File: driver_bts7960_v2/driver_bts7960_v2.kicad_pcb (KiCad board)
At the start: 2 copper layers, 56.4 x 50.7 mm, 31 parts, among them J1 Motor_1, J2 Alimentacion, J6 Motor_2, J7 Conn_02x04_Odd_Even, U1 BTS7960B, U2 BTS7960B, U3 BTS7960B, U4 BTS7960B

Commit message: v2
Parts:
- J1, J6: footprint Connector_AMASS:AMASS_XT30PW-M_1x02_P2.50mm_Horizontal -> Connector_AMASS:AMASS_XT30UPB-F_1x02_P5.0mm_Vertical
- moved REF** 9.10 mm to (161.7, 38.4)
- moved REF** 9.07 mm to (111.9, 38.4)
- moved C5 5.89 mm to (136.8, 72.5), turned to 0 degrees
- moved J2 4.63 mm to (152.1, 73.8)
- moved J7 3.45 mm to (127.7, 70.2)
- moved J1 1.46 mm to (128.6, 38.4), turned to 180 degrees
- moved J6 1.46 mm to (144.5, 38.4), turned to 180 degrees
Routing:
- net +24V: track 154.6 -> 86.3 mm
- net ENABLE_2: track 42.4 -> 48.5 mm
- net PWM_C: track 28.3 -> 33.3 mm
- net GND: track 160.3 -> 165.0 mm
- net PWM_B: track 14.2 -> 18.0 mm
- net PWM_A: track 5.91 -> 9.24 mm
- net PWM_D: track 14.1 -> 17.0 mm
- net Net-(J6-Pin_2): track 7.21 -> 8.67 mm
- net IS_1: track 51.2 -> 52.6 mm
- net Net-(J1-Pin_1): track 7.24 -> 8.66 mm
- net Net-(J1-Pin_2): track 22.1 -> 23.3 mm
- net Net-(J6-Pin_1): track 12.5 -> 13.6 mm
- net IS_2: track 79.2 -> 80.1 mm
- net ENABLE_1: track 21.3 -> 21.9 mm
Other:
- board size 56.4 x 50.7 mm -> 56.4 x 42.1 mm

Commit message: .
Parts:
- moved REF** 0.27 mm to (111.9, 73.6)
- moved REF** 0.21 mm to (161.7, 73.6)
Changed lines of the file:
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@@
 	(footprint "MountingHole:MountingHole_3.2mm_M3_DIN965_Pad_TopBottom"
 		(layer "F.Cu")
-		(at 111.7 73.775)
+		(at 111.9 73.6)
 		(descr "Mounting Hole 3.2mm, M3, DIN965")
 		(tags "mounting hole 3.2mm m3 din965")
@@
 	(footprint "MountingHole:MountingHole_3.2mm_M3_DIN965_Pad_TopBottom"
 		(layer "F.Cu")
-		(at 161.875 73.75)
+		(at 161.725 73.6)
 		(descr "Mounting Hole 3.2mm, M3, DIN965")
 		(tags "mounting hole 3.2mm m3 din965")
@@
 		(polygon
 			(pts
-				(xy 108.6 52.4695) (xy 159.3 51.963674) (xy 159.3 69.04) (xy 108.6 69.04)
+				(xy 108.6 52.4695) (xy 164.975 51.907056) (xy 164.975 76.87) (xy 108.6 76.87)
 			)
 		)

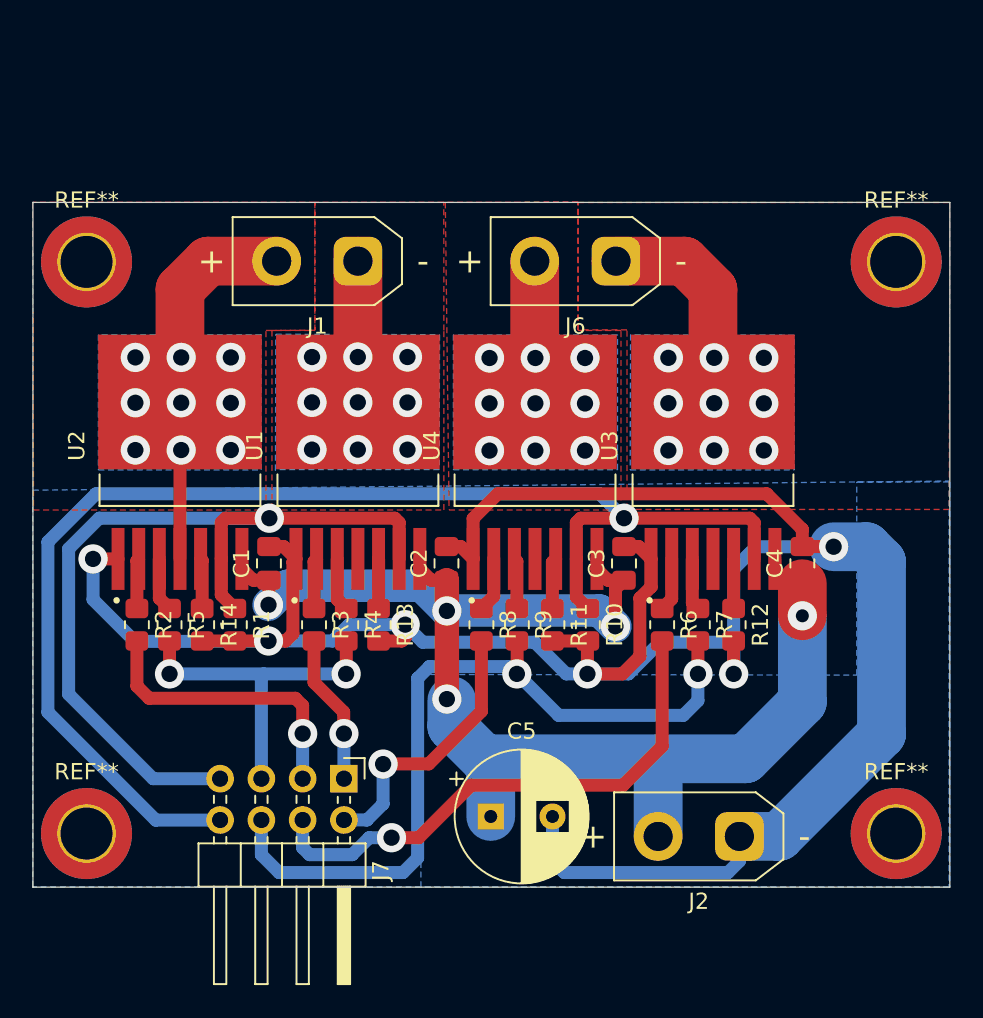
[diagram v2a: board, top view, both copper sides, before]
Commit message: v2 terminado con 74hc244
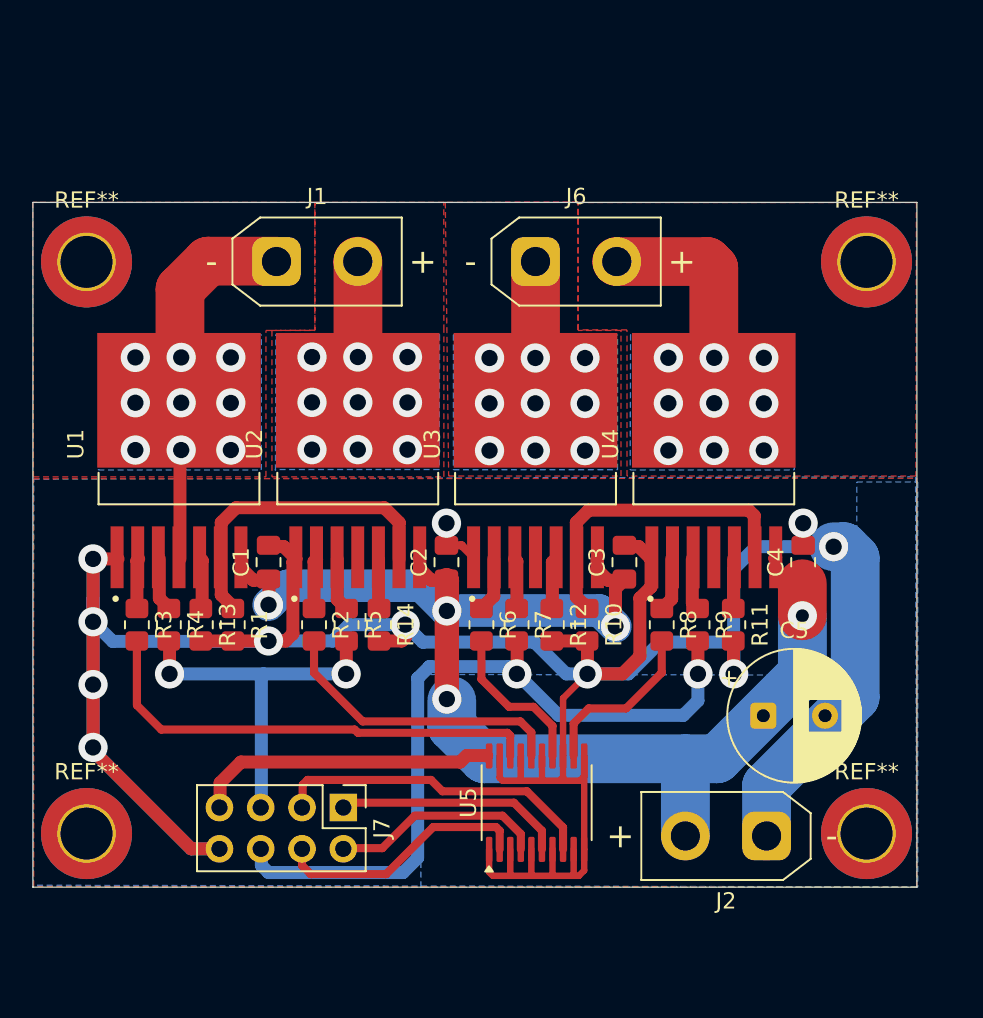
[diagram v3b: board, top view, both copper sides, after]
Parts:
- added U5: 74HC244, Package_SO:SSOP-20_4.4x6.5mm_P0.65mm, F.Cu at (139.6, 71.7)
- J7: footprint Connector_PinHeader_2.54mm:PinHeader_2x04_P2.54mm_Horizontal -> Connector_PinHeader_2.54mm:PinHeader_2x04_P2.54mm_Vertical
- moved C5 17.9 mm to (153.5, 66.3)
- moved R12 11.2 mm to (140.5, 60.8)
- moved R7 11.2 mm to (138.4, 60.8)
- moved R11 11.1 mm to (151.7, 60.8)
- moved R6 11.1 mm to (136.2, 60.8)
- moved R9 11.1 mm to (149.5, 60.8)
- moved R8 11.1 mm to (147.3, 60.8)
- moved U1 11.0 mm to (117.6, 50.6)
- moved U4 11.0 mm to (150.5, 50.6)
- moved U2 10.9 mm to (128.6, 50.6)
- moved R13 10.9 mm to (118.9, 60.8)
- moved U3 10.9 mm to (139.5, 50.6)
- moved R4 10.9 mm to (117.0, 60.8)
- moved R2 10.9 mm to (125.9, 60.8)
- moved R3 10.9 mm to (115.0, 60.8)
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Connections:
- J7 pad 1: PWM_A -> PWM_C
- J7 pad 2: PWM_D -> PWM_B
- J7 pad 3: PWM_B -> PWM_D
- J7 pad 4: PWM_C -> PWM_A
- J7 pad 7: IS_1 -> +5V
- J7 pad 8: IS_2 -> GND
- R1 pad 1: IS_1 -> Net-(U1-IS)
- R10 pad 1: IS_2 -> Net-(U3-IS)
- R2 pad 2: PWM_B -> OUT_B
- R3 pad 2: PWM_A -> OUT_A
- R6 pad 2: PWM_C -> OUT_C
- R8 pad 2: PWM_D -> OUT_D
- U1 pad 6: IS_1 -> Net-(U1-IS)
- U2 pad 6: IS_1 -> Net-(U1-IS)
- U3 pad 6: IS_2 -> Net-(U3-IS)
- U4 pad 6: IS_2 -> Net-(U3-IS)
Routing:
- net IS_2: track 80.1 -> 0.00 mm, vias 1 -> 0
- net IS_1: track 52.6 -> 0.00 mm, vias 1 -> 0
- net GND: track 165.0 -> 201.7 mm, vias 6 -> 11
- net OUT_A: track 0.00 -> 29.0 mm
- net Net-(U3-IS): track 0.00 -> 19.6 mm
- net Net-(U1-IS): track 0.00 -> 19.6 mm
- net PWM_C: track 33.3 -> 14.2 mm, vias 1 -> 0
- net +5V: track 0.00 -> 18.6 mm
- net OUT_B: track 0.00 -> 18.3 mm
- net Net-(J1-Pin_2): track 23.3 -> 8.66 mm
- net Net-(J1-Pin_1): track 8.66 -> 23.3 mm
- net OUT_D: track 0.00 -> 10.7 mm
- net OUT_C: track 0.00 -> 9.77 mm
- net PWM_A: track 9.24 -> 15.9 mm, vias 1 -> 0
- net Net-(J6-Pin_2): track 8.67 -> 14.3 mm
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- added copper zone on F.Cu, net GND
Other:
- board size 56.4 x 42.1 mm -> 54.4 x 42.1 mm

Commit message: .
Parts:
- moved J2 1.45 mm to (152.3, 73.8)
- moved REF** 1.15 mm to (158.8, 38.4)
- moved REF** 1.15 mm to (158.8, 73.5)
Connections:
- R4 pad 2: ENABLE_1 -> OUT_EN_1
- R5 pad 2: ENABLE_1 -> OUT_EN_1
- R7 pad 2: ENABLE_2 -> OUT_EN_2
- R9 pad 2: ENABLE_2 -> OUT_EN_2
- U5 pad 15: GND -> ENABLE_2
- U5 pad 17: GND -> ENABLE_1
- U5 pad 3: GND -> OUT_EN_1
- U5 pad 5: GND -> OUT_EN_2
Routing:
- net OUT_EN_2: track 0.00 -> 43.6 mm, vias 0 -> 3
- net OUT_EN_1: track 0.00 -> 39.3 mm, vias 0 -> 3
- net ENABLE_2: track 47.1 -> 32.3 mm, vias 2 -> 1
- net GND: track 201.7 -> 197.8 mm
- net +24V: track 81.8 -> 79.9 mm
- net PWM_C: track 14.2 -> 15.9 mm
- net PWM_D: track 20.1 -> 21.5 mm
- net PWM_A: track 15.9 -> 14.8 mm
- net OUT_C: track 9.77 -> 10.6 mm
- net ENABLE_1: track 23.7 -> 23.6 mm, vias 2 -> 1
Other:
- board size 54.4 x 42.1 mm -> 53.4 x 42.1 mm

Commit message: .
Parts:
- J2: value Alimentacion -> XT30

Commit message: .
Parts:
- J1, J6: footprint Connector_AMASS:AMASS_XT30UPB-F_1x02_P5.0mm_Vertical -> Connector_AMASS:AMASS_XT30U-F_1x02_P5.0mm_Vertical; moved to B.Cu
- J2: footprint Connector_AMASS:AMASS_XT30UPB-F_1x02_P5.0mm_Vertical -> Connector_AMASS:AMASS_XT30U-F_1x02_P5.0mm_Vertical
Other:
- board text added: "Made by Aiden MP"

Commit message: .
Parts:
- moved J7 0.65 mm to (127.1, 72.0)
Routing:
- net GND: track 197.8 -> 181.6 mm
- net ENABLE_2: track 32.3 -> 43.5 mm
- net OUT_EN_1: track 39.3 -> 37.5 mm
- net PWM_A: track 14.8 -> 16.2 mm, vias 0 -> 1
- net +5V: track 18.6 -> 20.1 mm, vias 0 -> 1
- net PWM_C: track 15.9 -> 16.5 mm, vias 0 -> 1
- net ENABLE_1: track 23.6 -> 24.3 mm
- net PWM_B: track 13.4 -> 13.8 mm, vias 0 -> 1
- net PWM_D: track 21.5 -> 21.7 mm, vias 0 -> 1
